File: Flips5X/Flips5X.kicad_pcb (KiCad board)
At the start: 2 copper layers, 100 x 100 mm, 23 parts, among them IC1 FP2800A, IC2 FP2800A, IC3 FP2800A

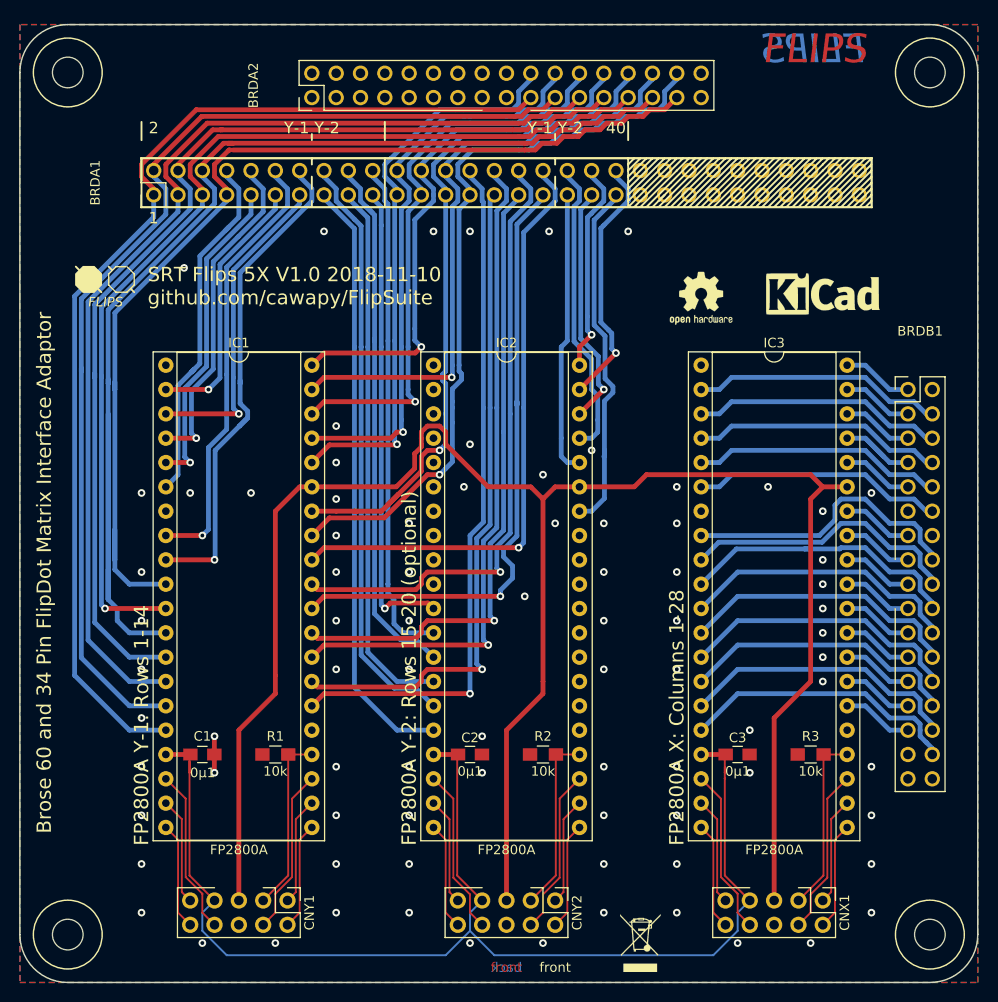
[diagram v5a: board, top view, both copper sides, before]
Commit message: Replace mounting holes: use variants with pad
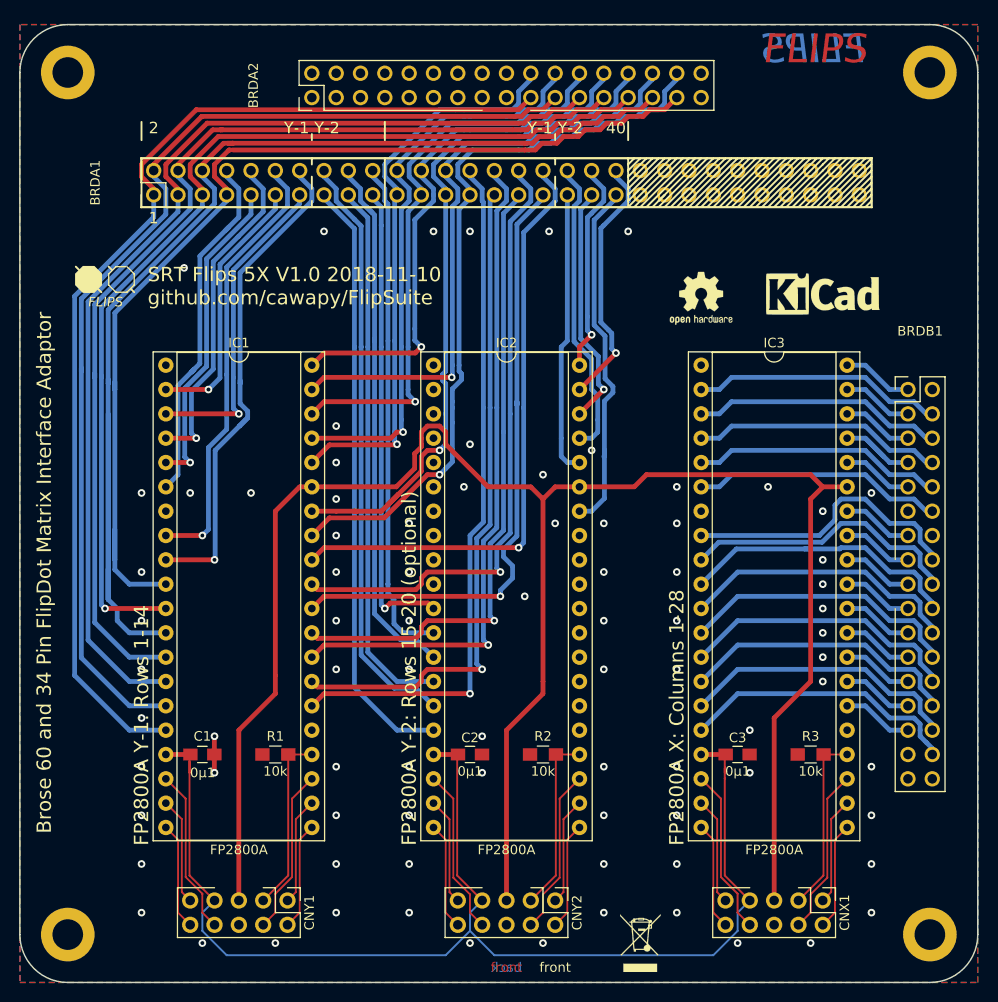
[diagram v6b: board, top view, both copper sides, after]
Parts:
- REF** (x4): value MountingHole_3.2mm_M3 -> MountingHole_3.2mm_M3_DIN965_Pad; footprint Mounting_Holes:MountingHole_3.2mm_M3 -> Mounting_Holes:MountingHole_3.2mm_M3_DIN965_Pad
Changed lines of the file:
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@@
     (add_net /~RY9)
+  )
+  (module Mounting_Holes:MountingHole_3.2mm_M3_DIN965_Pad (layer F.Cu)
+    (at 55.8 145.8)
+    (descr "Mounting Hole 3.2mm, M3, DIN965")
+    (tags "mounting hole 3.2mm m3 din965")
+    (attr virtual)
+    (fp_text reference REF** (at 0 -3.8) (layer F.Fab) hide
+      (effects (font (size 1 1) (thickness 0.15)))
+    )
+    (fp_text value MountingHole_3.2mm_M3_DIN965_Pad (at 0 3.8) (layer F.Fab)
+      (effects (font (size 1 1) (thickness 0.15)))
+    )
+    (fp_text user %R (at 0.3 0) (layer F.Fab)
+      (effects (font (size 1 1) (thickness 0.15)))
+    )
+    (fp_circle (center 0 0) (end 2.8 0) (layer Cmts.User) (width 0.15))
+    (fp_circle (center 0 0) (end 3.05 0) (layer F.CrtYd) (width 0.05))
+    (pad 1 thru_hole circle (at 0 0) (size 5.6 5.6) (drill 3.2) (layers *.Cu *.Mask))
+  )
+  (module Mounting_Holes:MountingHole_3.2mm_M3_DIN965_Pad (layer F.Cu)
+    (at 145.8 145.8)
+    (descr "Mounting Hole 3.2mm, M3, DIN965")
+    (tags "mounting hole 3.2mm m3 din965")
+    (attr virtual)
+    (fp_text reference REF** (at 0 -3.8) (layer F.Fab) hide
+      (effects (font (size 1 1) (thickness 0.15)))
+    )
+    (fp_text value MountingHole_3.2mm_M3_DIN965_Pad (at 0 3.8) (layer F.Fab)
+      (effects (font (size 1 1) (thickness 0.15)))
+    )
+    (fp_text user %R (at 0.3 0) (layer F.Fab)
+      (effects (font (size 1 1) (thickness 0.15)))
+    )
+    (fp_circle (center 0 0) (end 2.8 0) (layer Cmts.User) (width 0.15))
+    (fp_circle (center 0 0) (end 3.05 0) (layer F.CrtYd) (width 0.05))
+    (pad 1 thru_hole circle (at 0 0) (size 5.6 5.6) (drill 3.2) (layers *.Cu *.Mask))
+  )
+  (module Mounting_Holes:MountingHole_3.2mm_M3_DIN965_Pad (layer F.Cu)
+    (at 145.8 55.8)
+    (descr "Mounting Hole 3.2mm, M3, DIN965")
+    (tags "mounting hole 3.2mm m3 din965")
+    (attr virtual)
+    (fp_text reference REF** (at 0 -3.8) (layer F.Fab) hide
+      (effects (font (size 1 1) (thickness 0.15)))
+    )
+    (fp_text value MountingHole_3.2mm_M3_DIN965_Pad (at 0 3.8) (layer F.Fab)
+      (effects (font (size 1 1) (thickness 0.15)))
+    )
+    (fp_text user %R (at 0.3 0) (layer F.Fab)
+      (effects (font (size 1 1) (thickness 0.15)))
+    )
+    (fp_circle (center 0 0) (end 2.8 0) (layer Cmts.User) (width 0.15))
+    (fp_circle (center 0 0) (end 3.05 0) (layer F.CrtYd) (width 0.05))
+    (pad 1 thru_hole circle (at 0 0) (size 5.6 5.6) (drill 3.2) (layers *.Cu *.Mask))
+  )
+  (module Mounting_Holes:MountingHole_3.2mm_M3_DIN965_Pad (layer F.Cu)
+    (at 55.8 55.8)
+    (descr "Mounting Hole 3.2mm, M3, DIN965")
+    (tags "mounting hole 3.2mm m3 din965")
+    (attr virtual)
+    (fp_text reference REF** (at 0 -3.8) (layer F.Fab) hide
+      (effects (font (size 1 1) (thickness 0.15)))
+    )
+    (fp_text value MountingHole_3.2mm_M3_DIN965_Pad (at 0 3.8) (layer F.Fab)
+      (effects (font (size 1 1) (thickness 0.15)))
+    )
+    (fp_text user %R (at 0.3 0) (layer F.Fab)
+      (effects (font (size 1 1) (thickness 0.15)))
+    )
+    (fp_circle (center 0 0) (end 2.8 0) (layer Cmts.User) (width 0.15))
+    (fp_circle (center 0 0) (end 3.05 0) (layer F.CrtYd) (width 0.05))
+    (pad 1 thru_hole circle (at 0 0) (size 5.6 5.6) (drill 3.2) (layers *.Cu *.Mask))
   )
   (module Symbols:WEEE-Logo_4.2x6mm_SilkScreen (layer F.Cu)
@@
       (xy 1.530863 -2.420002) (xy 1.583231 -2.473048) (xy 2.125049 -3.022233) (xy 2.12443 -2.935152)) (layer F.SilkS) (width 0.01))
   )
-  (module Mounting_Holes:MountingHole_3.2mm_M3 (layer F.Cu)
-    (at 55.8 145.8)
-    (descr "Mounting Hole 3.2mm, no annular, M3")
-    (tags "mounting hole 3.2mm no annular m3")
-    (attr virtual)
-    (fp_text reference REF** (at 0 -4.2) (layer F.SilkS) hide
-      (effects (font (size 1 1) (thickness 0.15)))
-    )
-    (fp_text value MountingHole_3.2mm_M3 (at 0 4.2) (layer F.Fab)
-      (effects (font (size 1 1) (thickness 0.15)))
-    )
-    (fp_circle (center 0 0) (end 2.54 -2.54) (layer B.SilkS) (width 0.15))
-    (fp_circle (center 0 0) (end 2.54 -2.54) (layer F.SilkS) (width 0.15))
-    (fp_circle (center 0 0) (end 3.45 0) (layer F.CrtYd) (width 0.05))
-    (fp_circle (center 0 0) (end 3.2 0) (layer Cmts.User) (width 0.15))
-    (fp_text user %R (at 0.3 0) (layer F.Fab)
-      (effects (font (size 1 1) (thickness 0.15)))
-    )
-    (pad 1 np_thru_hole circle (at 0 0) (size 3.2 3.2) (drill 3.2) (layers *.Cu *.Mask))
-  )
-  (module Mounting_Holes:MountingHole_3.2mm_M3 (layer F.Cu)
-    (at 145.8 145.8)
-    (descr "Mounting Hole 3.2mm, no annular, M3")
-    (tags "mounting hole 3.2mm no annular m3")
-    (attr virtual)
-    (fp_text reference REF** (at 0 -4.2) (layer F.SilkS) hide
-      (effects (font (size 1 1) (thickness 0.15)))
-    )
-    (fp_text value MountingHole_3.2mm_M3 (at 0 4.2) (layer F.Fab)
-      (effects (font (size 1 1) (thickness 0.15)))
-    )
-    (fp_text user %R (at 0.3 0) (layer F.Fab)
-      (effects (font (size 1 1) (thickness 0.15)))
-    )
-    (fp_circle (center 0 0) (end 3.2 0) (layer Cmts.User) (width 0.15))
-    (fp_circle (center 0 0) (end 3.45 0) (layer F.CrtYd) (width 0.05))
-    (fp_circle (center 0 0) (end 2.54 -2.54) (layer F.SilkS) (width 0.15))
-    (fp_circle (center 0 0) (end 2.54 -2.54) (layer B.SilkS) (width 0.15))
-    (pad 1 np_thru_hole circle (at 0 0) (size 3.2 3.2) (drill 3.2) (layers *.Cu *.Mask))
-  )
-  (module Mounting_Holes:MountingHole_3.2mm_M3 (layer F.Cu)
-    (at 145.8 55.8)
-    (descr "Mounting Hole 3.2mm, no annular, M3")
-    (tags "mounting hole 3.2mm no annular m3")
-    (attr virtual)
-    (fp_text reference REF** (at 0 -4.2) (layer F.SilkS) hide
-      (effects (font (size 1 1) (thickness 0.15)))
-    )
-    (fp_text value MountingHole_3.2mm_M3 (at 0 4.2) (layer F.Fab)
-      (effects (font (size 1 1) (thickness 0.15)))
-    )
-    (fp_circle (center 0 0) (end 2.54 -2.54) (layer B.SilkS) (width 0.15))
-    (fp_circle (center 0 0) (end 2.54 -2.54) (layer F.SilkS) (width 0.15))
-    (fp_circle (center 0 0) (end 3.45 0) (layer F.CrtYd) (width 0.05))
-    (fp_circle (center 0 0) (end 3.2 0) (layer Cmts.User) (width 0.15))
-    (fp_text user %R (at 0.3 0) (layer F.Fab)
-      (effects (font (size 1 1) (thickness 0.15)))
-    )
-    (pad 1 np_thru_hole circle (at 0 0) (size 3.2 3.2) (drill 3.2) (layers *.Cu *.Mask))
-  )
-  (module Mounting_Holes:MountingHole_3.2mm_M3 (layer F.Cu)
-    (at 55.8 55.8)
-    (descr "Mounting Hole 3.2mm, no annular, M3")
-    (tags "mounting hole 3.2mm no annular m3")
-    (attr virtual)
-    (fp_text reference REF** (at 0 -4.2) (layer F.SilkS) hide
-      (effects (font (size 1 1) (thickness 0.15)))
-    )
-    (fp_text value MountingHole_3.2mm_M3 (at 0 4.2) (layer F.Fab)
-      (effects (font (size 1 1) (thickness 0.15)))
-    )
-    (fp_text user %R (at 0.3 0) (layer F.Fab)
-      (effects (font (size 1 1) (thickness 0.15)))
-    )
-    (fp_circle (center 0 0) (end 3.2 0) (layer Cmts.User) (width 0.15))
-    (fp_circle (center 0 0) (end 3.45 0) (layer F.CrtYd) (width 0.05))
-    (fp_circle (center 0 0) (end 2.54 -2.54) (layer F.SilkS) (width 0.15))
-    (fp_circle (center 0 0) (end 2.54 -2.54) (layer B.SilkS) (width 0.15))
-    (pad 1 np_thru_hole circle (at 0 0) (size 3.2 3.2) (drill 3.2) (layers *.Cu *.Mask))
-  )
   (module Housings_DIP:DIP-40_W15.24mm_Socket (layer F.Cu)
